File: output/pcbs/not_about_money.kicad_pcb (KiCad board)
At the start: 2 copper layers, 80 x 118 mm, 51 parts

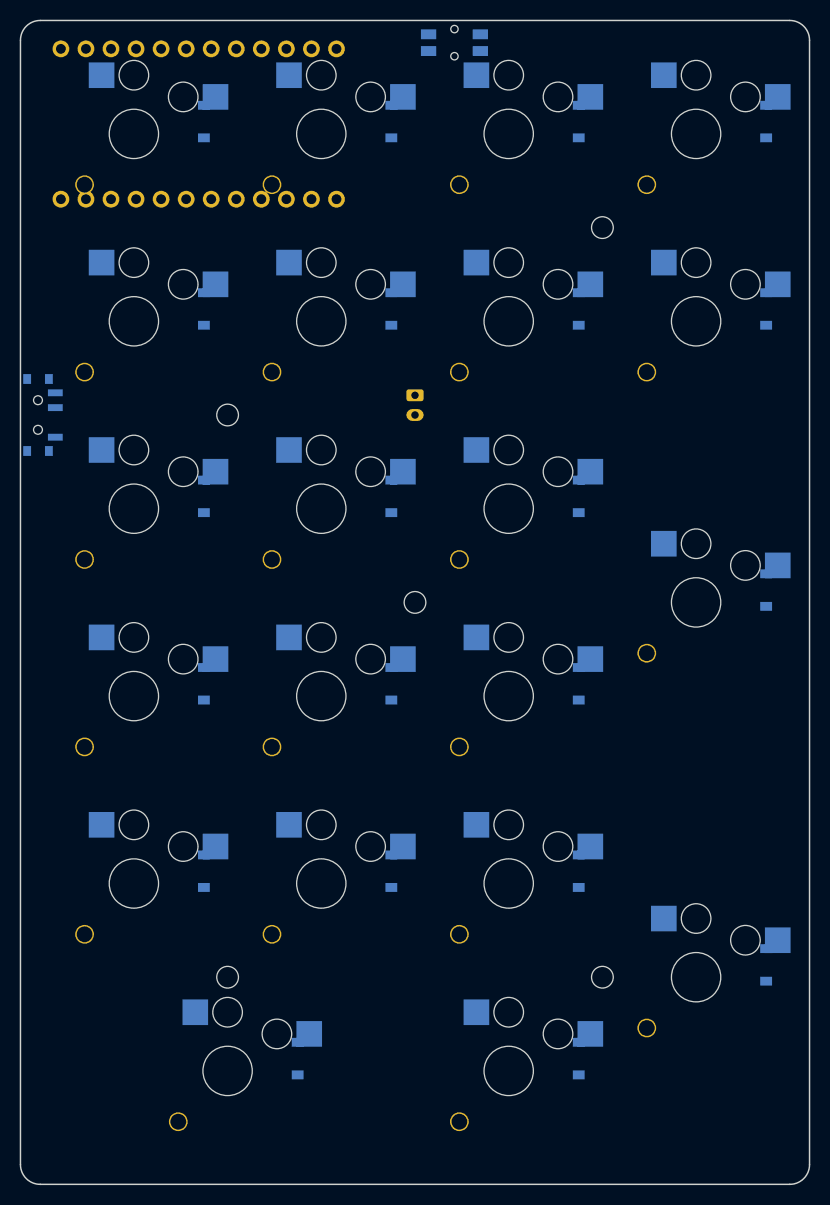
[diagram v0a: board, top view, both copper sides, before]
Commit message: Clean up: keep only the current design
- Remove the earlier design iterations (output_gateron, output_toplayout,
  output_keygap, output_led), the original choc output and the config /
  case-script backups; they remain in commit c19e498
- Move the current routed board from output_stabfix/ to output/
- Point case/build_case.py, README and CLAUDE.md at the new paths; warn
  against running ergogen with --clean on output/

Co-Authored-By: Claude Opus 5.5 <noreply@anthropic.com>
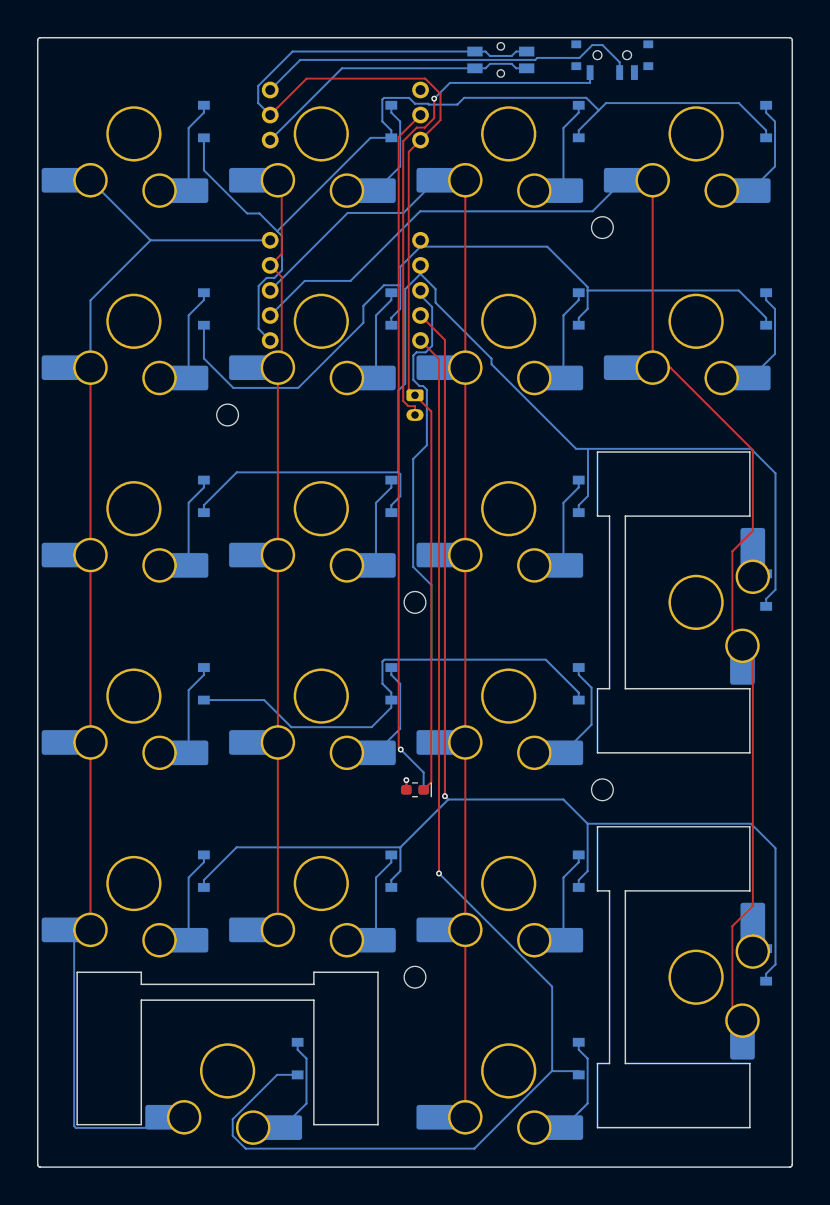
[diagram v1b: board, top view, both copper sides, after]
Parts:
- added LED1: , custom:smd_0603, F.Cu at (128.5, 71.5)
- added R1: , custom:smd_0603, B.Cu at (128.5, 71.5)
- S1, S10, S11, S12, S13, S14, S15, S16, S17, S18, S19, S2, S20, S21, S3, S4, S5, S6, S7, S8, S9: footprint ceoloide:switch_choc_v1_v2 -> ceoloide:switch_gateron_ks27_ks33
- moved S11 96.9 mm to (138.0, 100.0)
- moved S18 85.5 mm to (157.0, 5.00)
- moved S6 78.3 mm to (119.0, 81.0)
- moved PWR1 68.7 mm to (148.5, -2.96), turned to 90 degrees
- moved S19 67.2 mm to (109.5, 100.0)
- moved S20 66.5 mm to (157.0, 90.5), turned to 90 degrees
- moved S21 47.5 mm to (157.0, 52.5), turned to 90 degrees
- moved S17 26.9 mm to (157.0, 24.0)
- moved S1 21.2 mm to (100.0, 81.0)
- moved MH3 19.0 mm to (147.5, 71.5)
- moved MH4 19.0 mm to (128.5, 90.5)
- moved S10 19.0 mm to (119.0, 5.00)
- moved S12 19.0 mm to (138.0, 81.0)
- moved S13 19.0 mm to (138.0, 62.0)
- moved S14 19.0 mm to (138.0, 43.0)
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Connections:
- D1 pad 1: (no net) -> R6
- D10 pad 1: (no net) -> R2
- D11 pad 1: (no net) -> R1
- D12 pad 1: (no net) -> R6
- D13 pad 1: (no net) -> R5
- D14 pad 1: (no net) -> R4
- D15 pad 1: (no net) -> R3
- D16 pad 1: (no net) -> R2
- D17 pad 1: (no net) -> R1
- D18 pad 1: (no net) -> R5
- D19 pad 1: (no net) -> R3
- D2 pad 1: (no net) -> R5
- D20 pad 1: (no net) -> R2
- D21 pad 1: (no net) -> R1
- D3 pad 1: (no net) -> R4
- D4 pad 1: (no net) -> R3
- D5 pad 1: (no net) -> R2
- D6 pad 1: (no net) -> R1
- D7 pad 1: (no net) -> R5
- D8 pad 1: (no net) -> R4
- D9 pad 1: (no net) -> R3
- MCU1 pad 10: R3 -> R5
- MCU1 pad 11: R4 -> R6
- MCU1 pad 15: C6 -> C4
- MCU1 pad 16: C5 -> C3
- MCU1 pad 17: C4 -> C2
- MCU1 pad 18: C3 -> C1
- MCU1 pad 7: P4 -> R2
- MCU1 pad 8: P5 -> R3
- MCU1 pad 9: P6 -> R4
- S1 pad 1: (no net) -> C1
- S1 pad 2: c1_r6 -> c1_r5
- S10 pad 1: (no net) -> C2
- S10 pad 2: c2_r2 -> c2_r1
- S11 pad 1: (no net) -> C3
- S11 pad 2: c2_r1 -> c3_r6
- S12 pad 1: (no net) -> C3
- S12 pad 2: c3_r6 -> c3_r5
- S13 pad 1: (no net) -> C3
- S13 pad 2: c3_r5 -> c3_r4
- S14 pad 1: (no net) -> C3
- S14 pad 2: c3_r4 -> c3_r3
- S15 pad 1: (no net) -> C3
- S15 pad 2: c3_r3 -> c3_r2
- S16 pad 1: (no net) -> C3
- S16 pad 2: c3_r2 -> c3_r1
- S17 pad 1: (no net) -> C4
- S17 pad 2: c3_r1 -> c4_r2
- S18 pad 1: (no net) -> C4
- S18 pad 2: c4_r5 -> c4_r1
- S19 pad 1: (no net) -> C1
- S19 pad 2: c4_r3 -> c1_r6
- S2 pad 1: (no net) -> C1
- S2 pad 2: c1_r5 -> c1_r4
- S20 pad 1: (no net) -> C4
- S20 pad 2: c4_r2 -> c4_r5
- S21 pad 1: (no net) -> C4
- S21 pad 2: c4_r1 -> c4_r3
- S3 pad 1: (no net) -> C1
- S3 pad 2: c1_r4 -> c1_r3
- S4 pad 1: (no net) -> C1
- S4 pad 2: c1_r3 -> c1_r2
- S5 pad 1: (no net) -> C1
- S5 pad 2: c1_r2 -> c1_r1
- S6 pad 1: (no net) -> C2
- S6 pad 2: c1_r1 -> c2_r5
- S7 pad 1: (no net) -> C2
- S7 pad 2: c2_r5 -> c2_r4
- S8 pad 1: (no net) -> C2
- S8 pad 2: c2_r4 -> c2_r3
- S9 pad 1: (no net) -> C2
- S9 pad 2: c2_r3 -> c2_r2
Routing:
- net C4: track 0.00 -> 145.8 mm
- net R5: track 0.00 -> 139.5 mm, vias 0 -> 1
- net C1: track 0.00 -> 139.5 mm
- net C3: track 0.00 -> 134.2 mm
- net R6: track 0.00 -> 129.0 mm, vias 0 -> 1
- net GND: track 0.00 -> 125.1 mm
- net R3: track 0.00 -> 114.6 mm
- net R1: track 0.00 -> 92.2 mm
- net C2: track 0.00 -> 92.0 mm
- net R4: track 0.00 -> 89.5 mm
- net R2: track 0.00 -> 82.5 mm
- net P0: track 0.00 -> 70.4 mm, vias 0 -> 1
- net BAT_P: track 0.00 -> 52.3 mm, vias 0 -> 1
- net RAW: track 0.00 -> 39.1 mm
- net RST: track 0.00 -> 29.4 mm
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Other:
- board size 80 x 118 mm -> 76.5 x 114.5 mm
